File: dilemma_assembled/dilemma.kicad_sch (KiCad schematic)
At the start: 106 parts, among them J1 USB_C_Receptacle_USB2.0, J102 Serial, J103 Serial, J105 Conn_01x04_Female, J107 Conn_01x08_Female, J108 Conn_01x01_Female, J109 Conn_01x01_Female, J113 Cirque, J5 Conn_01x02, SW1 SW_Push, SW101 SW_Push, SW102 SW_Push, SW103 SW_Push, SW104 SW_Push, SW105 SW_Push, SW106 SW_Push, SW107 SW_Push, SW108 SW_Push, SW109 SW_Push, SW110 SW_SPST, SW111 SW_SPST, SW112 SW_Push, SW113 SW_Push, SW114 SW_Push, SW115 SW_Push, SW116 SW_Push, SW117 SW_Push, SW118 SW_Push, SW119 SW_Push, SW2 SW_Push, U1 RP2040, U2 GD25Q80CEIGR, U3 XC6210B332MR-G, Y1 Crystal_GND24

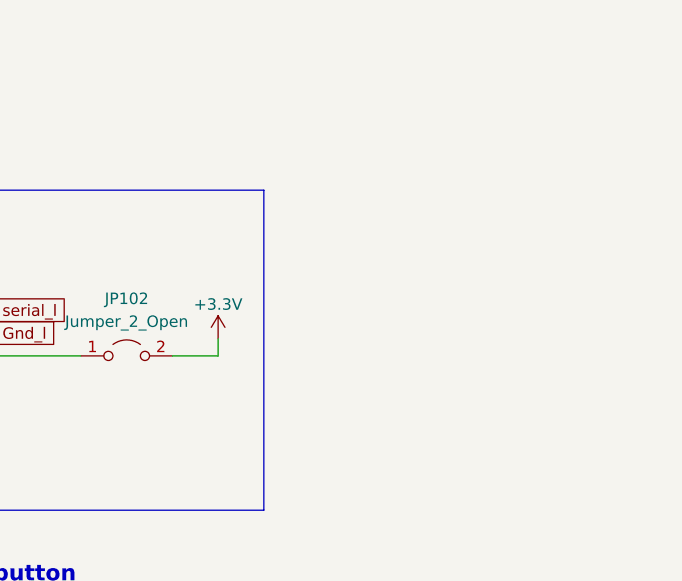
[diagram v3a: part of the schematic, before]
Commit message: add back tenting puck
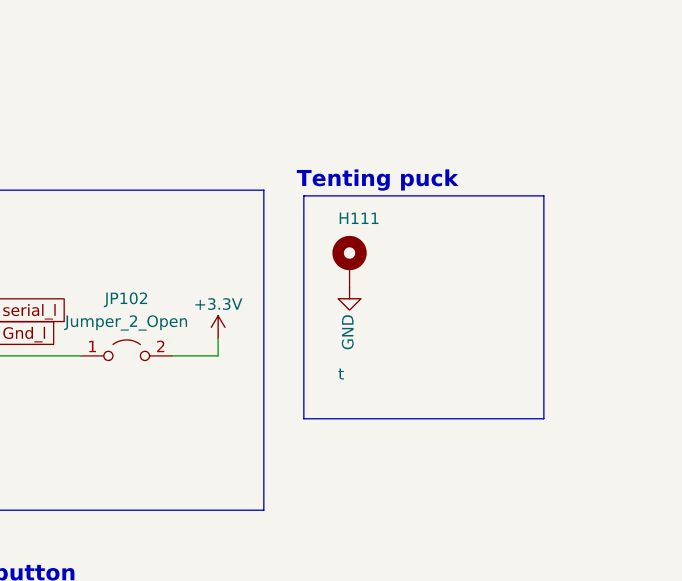
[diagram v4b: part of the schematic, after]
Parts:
- added H111: t, local-libraries:Tenting_Puck, symbol Mechanical:MountingHole_Pad
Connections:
- net GND: now also H111.1
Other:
- note added: "Tenting puck"
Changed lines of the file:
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@@
     (stroke (width 0) (type default) (color 0 0 0 0))
   )
+  (polyline (pts (xy 348.615 167.005) (xy 348.615 191.77))
+    (stroke (width 0) (type default) (color 0 0 0 0))
+  )
   (wire (pts (xy 171.45 38.1) (xy 171.45 40.64))
     (stroke (width 0) (type default) (color 0 0 0 0))
@@
     (stroke (width 0) (type default) (color 0 0 0 0))
   )
+  (polyline (pts (xy 348.615 167.005) (xy 375.285 167.005))
+    (stroke (width 0) (type default) (color 0 0 0 0))
+  )
   (wire (pts (xy 318.77 61.595) (xy 321.31 61.595))
     (stroke (width 0) (type default) (color 0 0 0 0))
@@
     (stroke (width 0) (type default) (color 0 0 0 0))
   )
+  (polyline (pts (xy 375.285 167.005) (xy 375.285 191.77))
+    (stroke (width 0) (type default) (color 0 0 0 0))
+  )
   (wire (pts (xy 285.623 222.25) (xy 291.338 222.25))
     (stroke (width 0) (type default) (color 0 0 0 0))
@@
     (stroke (width 0) (type default) (color 0 0 0 0))
   )
+  (polyline (pts (xy 375.285 191.77) (xy 348.615 191.77))
+    (stroke (width 0) (type default) (color 0 0 0 0))
+  )
   (wire (pts (xy 138.43 40.64) (xy 138.43 38.1))
     (stroke (width 0) (type default) (color 0 0 0 0))
@@
     (effects (font (size 1.778 1.778) (thickness 0.3556) bold) (justify left bottom))
   )
+  (text "Tenting puck" (at 365.76 166.37 180)
+    (effects (font (size 1.778 1.778) (thickness 0.3556) bold) (justify right bottom))
+  )
   (text "Plate screws" (at 197.485 167.005 180)
     (effects (font (size 1.778 1.778) (thickness 0.3556) bold) (justify right bottom))
@@
     )
   )
+  (symbol (lib_id "power:GND") (at 353.695 177.165 0) (unit 1)
+    (in_bom yes) (on_board yes)
+    (property "Reference" "#PWR0124" (id 0) (at 353.695 183.515 0)
+      (effects (font (size 1.27 1.27)) hide)
+    )
+    (property "Value" "GND" (id 1) (at 353.539 184.1499 90)
+      (effects (font (size 1.27 1.27)) (justify left))
+    )
+    (property "Footprint" "" (id 2) (at 353.695 177.165 0)
+      (effects (font (size 1.27 1.27)) hide)
+    )
+    (property "Datasheet" "" (id 3) (at 353.695 177.165 0)
+      (effects (font (size 1.27 1.27)) hide)
+    )
+    (pin "1")
+  )
   (symbol (lib_id "Device:C") (at 148.59 180.34 0) (unit 1)
     (in_bom yes) (on_board yes)
@@
       (effects (font (size 1.27 1.27)) hide)
     )
-    (pin "14")
-    (pin "8")
-    (pin "9")
+    (pin "1")
     (pin "10")
     (pin "11")
     (pin "12")
     (pin "13")
-    (pin "1")
+    (pin "14")
     (pin "2")
     (pin "3")
@@
     (pin "6")
     (pin "7")
+    (pin "8")
+    (pin "9")
   )
   (symbol (lib_id "Mechanical:MountingHole_Pad") (at 220.345 176.53 0) (unit 1)
@@
     (pin "2")
   )
+  (symbol (lib_id "Mechanical:MountingHole_Pad") (at 353.695 174.625 0) (unit 1)
+    (in_bom yes) (on_board yes)
+    (property "Reference" "H111" (id 0) (at 352.425 169.545 0)
+      (effects (font (size 1.27 1.27)) (justify left))
+    )
+    (property "Value" "t" (id 1) (at 352.425 186.817 0)
+      (effects (font (size 1.27 1.27)) (justify left))
+    )
+    (property "Footprint" "local-libraries:Tenting_Puck" (id 2) (at 353.695 174.625 0)
+      (effects (font (size 1.27 1.27)) hide)
+    )
+    (property "Datasheet" "~" (id 3) (at 353.695 174.625 0)
+      (effects (font (size 1.27 1.27)) hide)
+    )
+    (pin "1")
+  )
   (sheet_instances
     (path "/" (page "1"))
@@
       (reference "#PWR0123") (unit 1) (value "GND") (footprint "")
     )
+    (path "/021ed89a-ca5a-454a-8f0d-f9d80781599b"
+      (reference "#PWR0124") (unit 1) (value "GND") (footprint "")
+    )
     (path "/4a21e78b-0ab0-4b88-8132-9b174e045719"
       (reference "C1") (unit 1) (value "1µ") (footprint "Capacitor_SMD:C_0603_1608Metric")
@@
       (reference "H110") (unit 1) (value "t") (footprint "local-libraries:JLC_SMT_Assembly_Hole")
     )
+    (path "/fe1fc527-60b6-4641-947d-42c4e081bc8b"
+      (reference "H111") (unit 1) (value "t") (footprint "local-libraries:Tenting_Puck")
+    )
     (path "/6125bb34-31fe-49ed-b2ab-61dab24d450a"

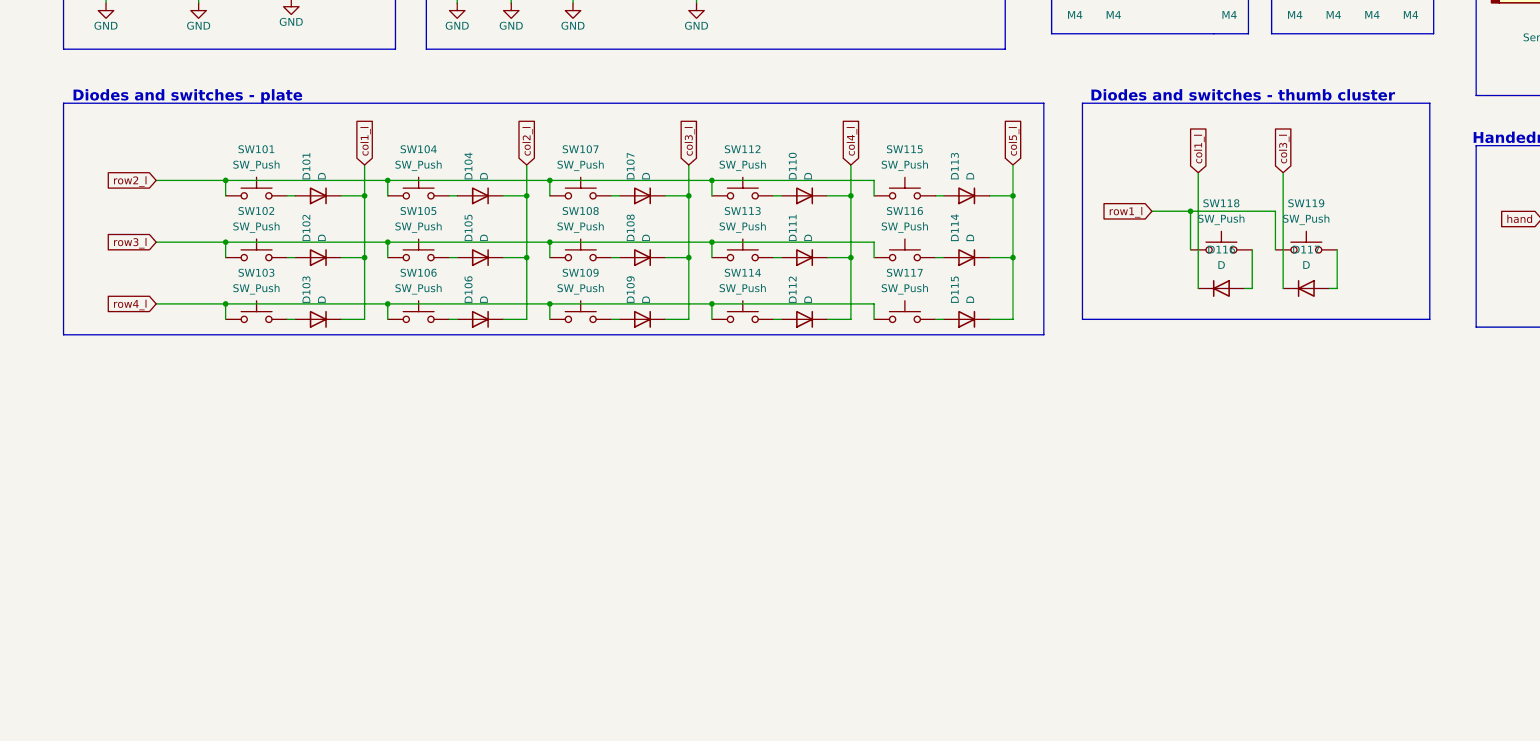
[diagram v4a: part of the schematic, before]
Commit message: add thumb key and encoder
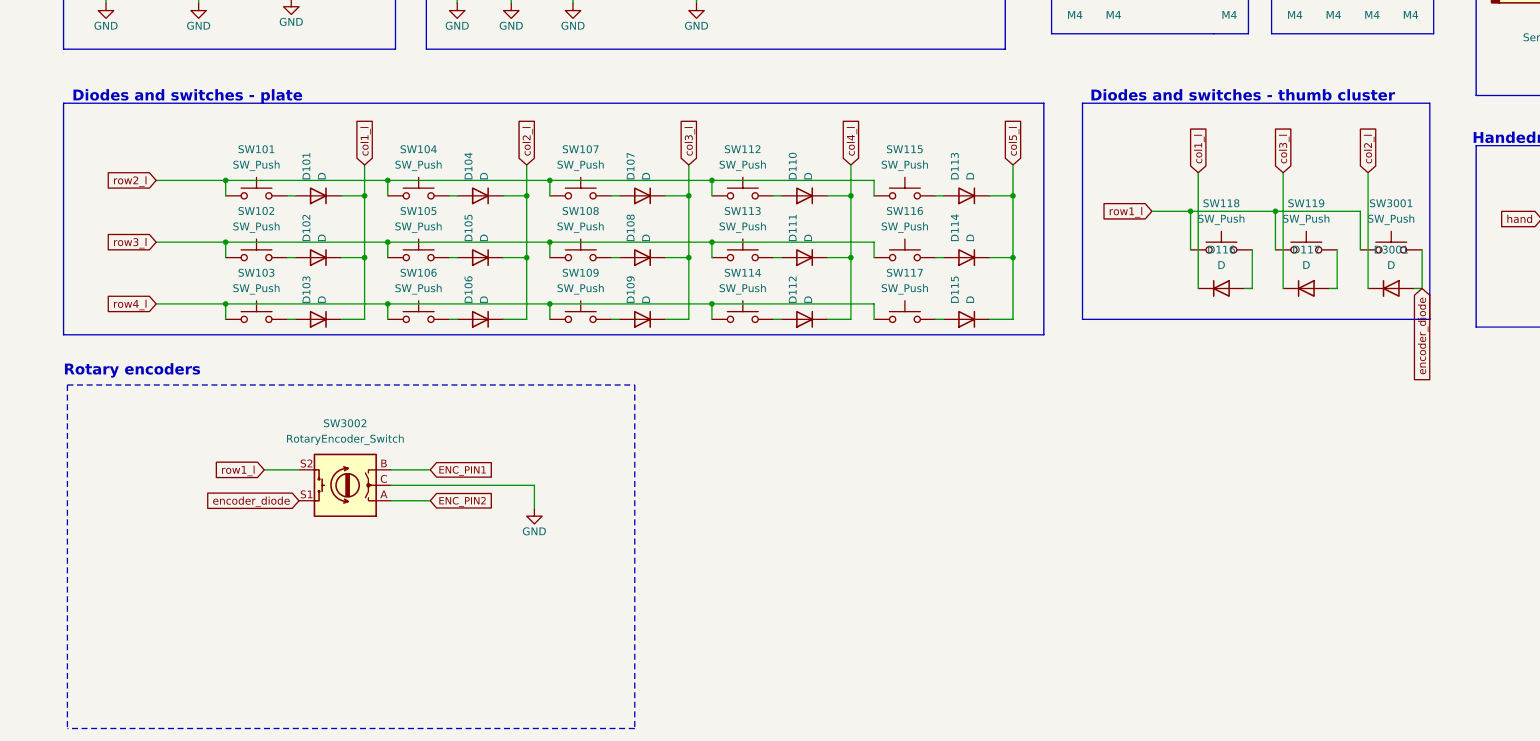
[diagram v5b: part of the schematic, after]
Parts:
- added D3001: D, local-libraries:D_1206_handsolder_reversible, symbol Device:D
- added SW3001: SW_Push, local-libraries:SW_MX_choc, symbol Switch:SW_Push
- added SW3002: RotaryEncoder_Switch, local-libraries:RotaryEncoder_Alps_EC11E-Switch_Vertical_H20mm_roundholes, symbol Device:RotaryEncoder_Switch
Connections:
- net GND: now also SW3002.C
- net col2_l: now also D3001.1 (K)
- net row1_l: now also SW3001.1, SW3002.S2
- new net ENC_PIN1: SW3002.B
- new net ENC_PIN2: SW3002.A
- new net encoder_diode: D3001.2 (A), SW3001.2, SW3002.S1
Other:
- note added: "Rotary encoders"

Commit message: cleanup schematic
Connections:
- net GND: no longer J102.R1, J103.R1, J105.4 (Pin_4), J107.2 (Pin_2), J113.11 (Pin_11), JP109.1 (A), JP110.1 (A), JP111.2 (B), SW110.2 (B), SW111.2 (B)
- net D12: no longer names the net of U1.15 (GPIO12)
- net D13: no longer names the net of U1.16 (GPIO13)
- net D14: no longer names the net of U1.17 (GPIO14)
- net D15: no longer names the net of U1.18 (GPIO15)
- net D16: no longer names the net of U1.27 (GPIO16)
- net Rst_l renamed ~{RESET}
- net col1_l renamed M_COL1
- net col2_l renamed M_COL2
- net col3_l renamed M_COL3
- net col4_l renamed M_COL4
- net col5_l renamed M_COL5
- net hand renamed HAND
- net miso_l renamed MISO
- net mosi_l renamed MOSI
- net row1_l renamed M_ROW1
- net row2_l renamed M_ROW2
- net row3_l renamed M_ROW3
- net row4_l renamed M_ROW4
- net sc_l renamed SCLK
- net scl_l renamed SCL
- net sda_l renamed SDA
- net serial_l renamed SERIAL
- new net Gnd_l: J102.R1, J103.R1, J105.4 (Pin_4), J107.2 (Pin_2), J113.11 (Pin_11), JP109.1 (A), JP110.1 (A), JP111.2 (B), SW110.2 (B), SW111.2 (B)
- no-connect marks 20 -> 15
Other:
- note removed: "Board IO headers"

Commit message: switch switches
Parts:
- removed J103: Serial, local-libraries:Jack_3.5mm_PJ320E_Horizontal_custom, symbol Connector:AudioJack4
- removed J107: Conn_01x08_Female, local-libraries:1x08 smd reversible, symbol Connector:Conn_01x08_Female
- removed JP101, JP102, JP103, JP104, JP105, JP106, JP107, JP108, JP109, JP110: Jumper_2_Open, local-libraries:SolderJumper-2_P1.3mm_Open_RoundedPad1.0x1.5mm, symbol Jumper:Jumper_2_Open
- J102: footprint local-libraries:Jack_3.5mm_PJ320E_Horizontal_custom -> local-libraries:Jack_3.5mm_PJ320E_Horizontal
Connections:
- net +3V3: now also J102.T, O101.2 (Pin_2)
- net GND: now also J102.R1, J105.4 (Pin_4), J113.11 (Pin_11), O101.1 (Pin_1), SW110.2 (B), SW111.2 (B)
- net SCL: now also O101.3 (Pin_3)
- net SDA: now also O101.4 (Pin_4)
- removed net Gnd_l: J102.R1, J105.4 (Pin_4), J113.11 (Pin_11), JP111.2 (B), SW110.2 (B), SW111.2 (B)
- no-connect marks 15 -> 19
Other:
- note removed: "I2C breakout"
- moved on the sheet: H103, H109, H110, J105, J108, J109, J113, O101, R103, R104

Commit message: routing
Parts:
- removed J108, J109: Conn_01x01_Female, Connector_Wire:SolderWirePad_1x01_SMD_1x2mm, symbol Connector:Conn_01x01_Female
- removed JP111, JP112: Jumper_2_Open, local-libraries:SolderJumper-2_P1.3mm_Open_RoundedPad1.0x1.5mm, symbol Jumper:Jumper_2_Open
- removed SW111: SW_SPST, local-libraries:SW_Push_1P1T_NO_6x6mm_H9.5mm, symbol Switch:SW_SPST
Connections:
- net +3V3: now also R101.2
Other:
- note added: "switch to gnd for left half"
- note removed: "GPIO breakout"
